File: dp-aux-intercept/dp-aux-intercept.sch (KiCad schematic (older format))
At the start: 29 parts

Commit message: Assigning footprints to AUX select headers.
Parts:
- JCAUXN1, JCAUXP1, JDAUXN1, JDAUXP1: footprint (none) -> Pin_Headers:Pin_Header_Straight_1x03
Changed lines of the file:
@@
 F 0 "JCAUXP1" V 3950 4340 50  0000 C CNN
 F 1 "CONN_01X03" V 3950 4340 50  0001 C CNN
-F 2 "" H 3850 4340 60  0001 C CNN
+F 2 "Pin_Headers:Pin_Header_Straight_1x03" H 3850 4340 60  0001 C CNN
 F 3 "" H 3850 4340 60  0000 C CNN
 	1    3850 4340
@@
 F 0 "JCAUXN1" V 3950 5080 50  0000 C CNN
 F 1 "CONN_01X03" V 3950 5080 50  0001 C CNN
-F 2 "" H 3850 5080 60  0001 C CNN
+F 2 "Pin_Headers:Pin_Header_Straight_1x03" H 3850 5080 60  0001 C CNN
 F 3 "" H 3850 5080 60  0000 C CNN
 	1    3850 5080
@@
 F 0 "JDAUXP1" V 5880 4340 50  0000 C CNN
 F 1 "CONN_01X03" V 5890 4340 50  0001 C CNN
-F 2 "" H 5790 4340 60  0001 C CNN
+F 2 "Pin_Headers:Pin_Header_Straight_1x03" H 5790 4340 60  0001 C CNN
 F 3 "" H 5790 4340 60  0000 C CNN
 	1    5790 4340
@@
 F 0 "JDAUXN1" V 5880 5080 50  0000 C CNN
 F 1 "CONN_01X03" V 5890 5080 50  0001 C CNN
-F 2 "" H 5790 5080 60  0001 C CNN
+F 2 "Pin_Headers:Pin_Header_Straight_1x03" H 5790 5080 60  0001 C CNN
 F 3 "" H 5790 5080 60  0000 C CNN
 	1    5790 5080

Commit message: Temp commit.
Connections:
- net CAUX_N is gone; now on net CAUX1_N: CCAN1.2, DPC1.17 (AUXCH_N), RCAN1.2
- net CAUX_P is gone; now on net CAUX1_P: CCAP1.2, DPC1.15 (AUXCH_P), RCAP1.1
- net DAUX_N is gone; now on net DAUX1_N: CDAN1.1, DPD1.17 (AUXCH_N), RDAN1.2
- net DAUX_P is gone; now on net DAUX1_P: CDAP1.1, DPD1.15 (AUXCH_P), RDAP1.1
- net CAUX2_P: now reaches CCAP1.1, JCAUXP1.2 (P2), RCAP2.1
- net CAUX2_N: now reaches CCAN1.1, JCAUXN1.2 (P2), RCAN2.2
- net DAUX2_P: now reaches CDAP1.2, JDAUXP1.2 (P2), RDAP2.1
- net DAUX2_N: now reaches CDAN1.2, JDAUXN1.2 (P2), RDAN2.2
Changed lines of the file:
@@
 Text Label 2050 2640 0    60   ~ 0
 CAUX_P
-Text Label 2500 5080 0    60   ~ 0
-CAUX_N
+Text Label 2500 5080 0    39   ~ 0
+CAUX1_N
 Text Label 7270 2640 0    60   ~ 0
 DAUX_P
@@
 	0    -1   -1   0
 $EndComp
-Text Notes 2780 4200 0    60   ~ 0
+Text Notes 2710 4130 0    60   ~ 0
 DisplayPort Sink\n    Biasing
 Text Notes 760  930  0    60   ~ 0
@@
 Wire Wire Line
 	2480 2640 2480 4340
-Text Label 2500 4340 0    60   ~ 0
-CAUX_P
+Text Label 2500 4340 0    39   ~ 0
+CAUX1_P
 $Comp
 L VDD #PWR08
@@
 	5700 4740 5700 4540
 Connection ~ 5700 4540
-Text Label 6860 4340 0    60   ~ 0
-DAUX_P
-Text Label 6860 5080 0    60   ~ 0
-DAUX_N
-Text Notes 6110 4210 0    60   ~ 0
+Text Label 6860 4340 0    39   ~ 0
+DAUX1_P
+Text Label 6860 5080 0    39   ~ 0
+DAUX1_N
+Text Notes 6220 4170 0    60   ~ 0
 DisplayPort Source\n      Biasing
 Connection ~ 7630 3040
@@
 Text Label 4290 3840 0    60   ~ 0
 CHPD
+Text Label 3480 4340 1    39   ~ 0
+CAUX2_P
+Text Label 3490 5080 3    39   ~ 0
+CAUX2_N
+Text Label 6180 5080 3    39   ~ 0
+DAUX2_N
+Text Label 6170 4340 1    39   ~ 0
+DAUX2_P
 $EndSCHEMATC

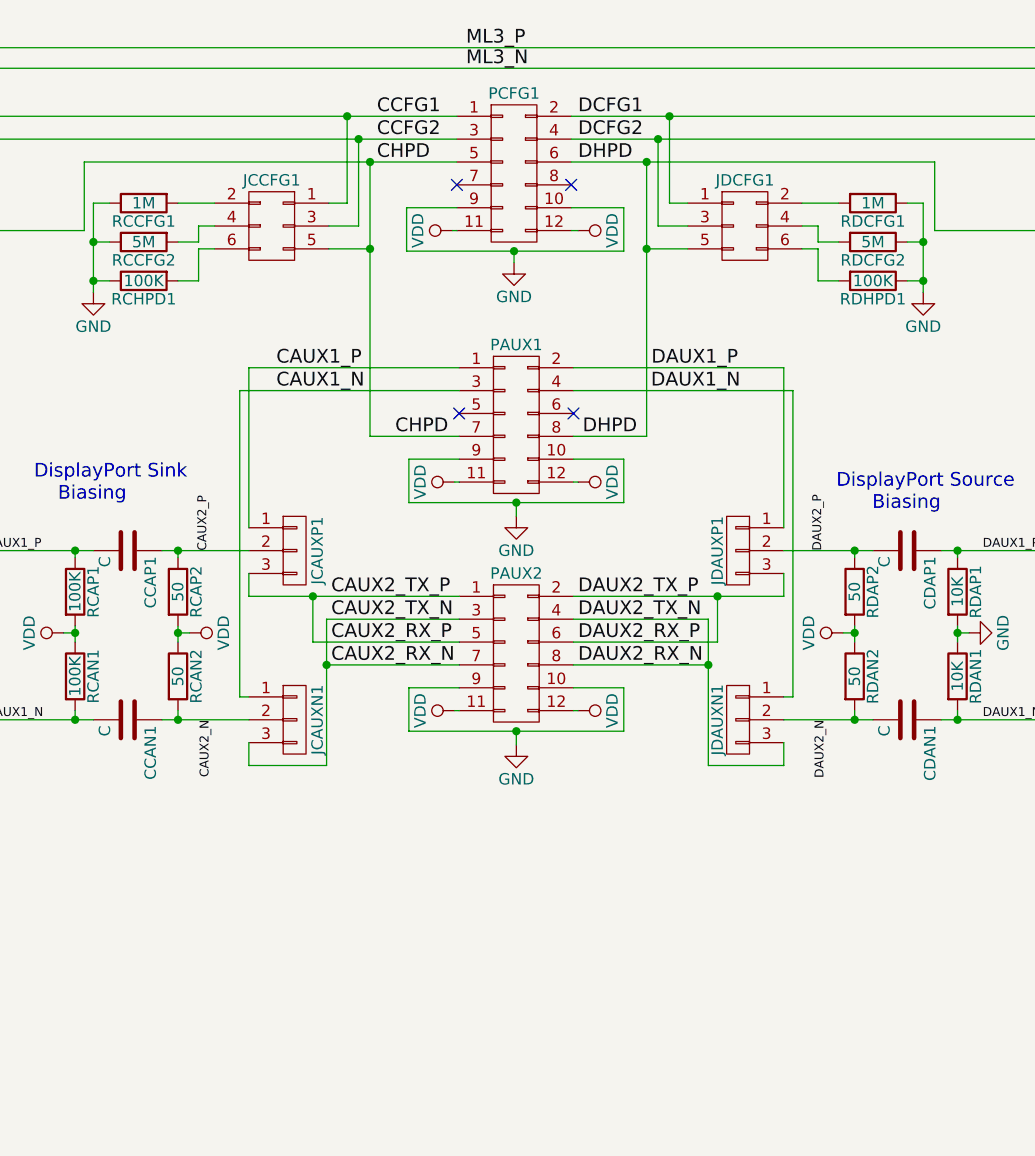
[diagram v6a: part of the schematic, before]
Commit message: Alternative method of two PMOD styles.
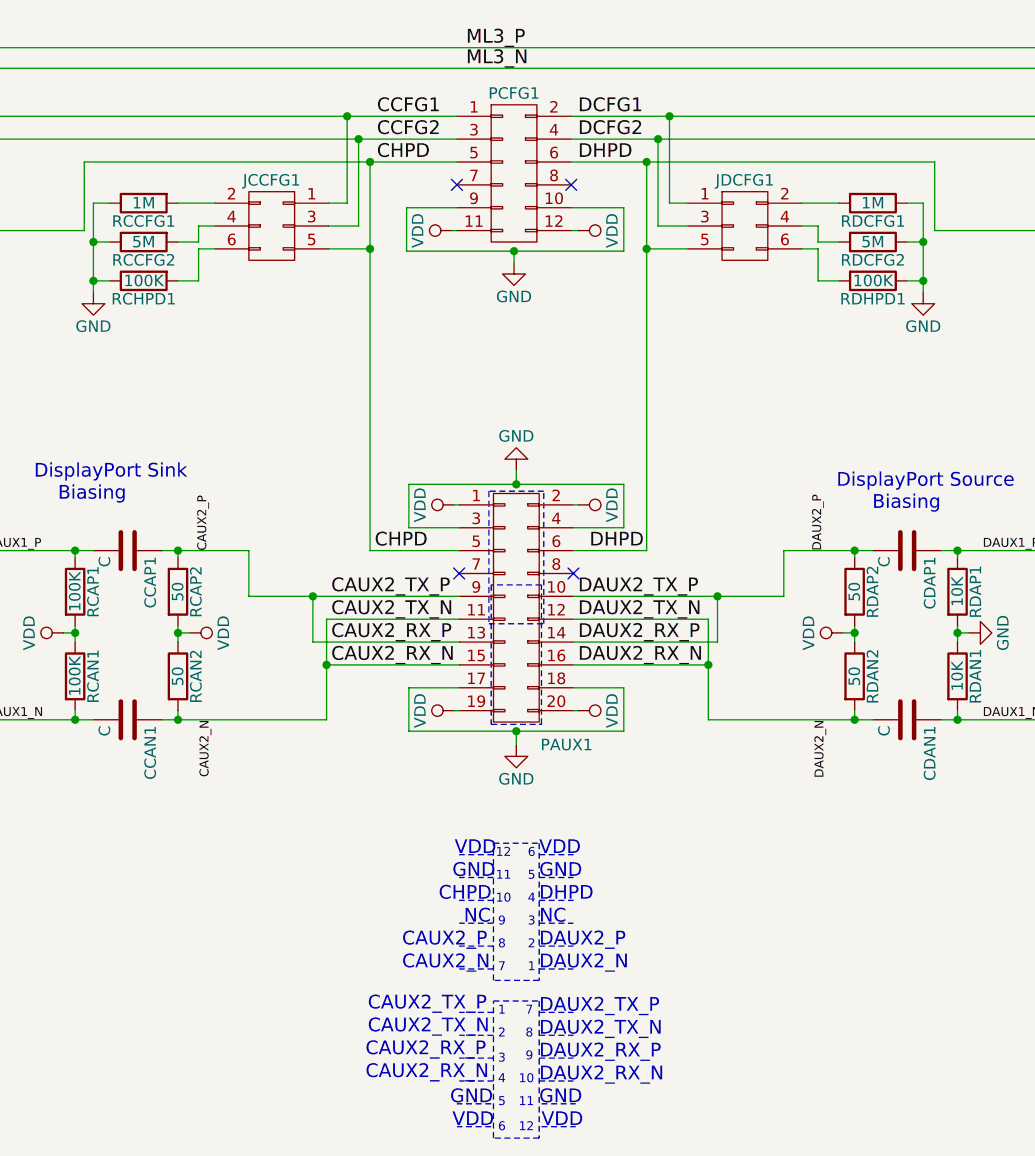
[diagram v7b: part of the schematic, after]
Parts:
- removed JCAUXN1, JCAUXP1, JDAUXN1, JDAUXP1: CONN_01X03, Pin_Headers:Pin_Header_Straight_1x03, symbol CONN_01X03
- removed PAUX1, PAUX2: CONN_02X06, Pin_Headers:Pin_Header_Angled_2x06, symbol CONN_02X06
- added PAUX1: CONN_02X10, Socket_Strips:Socket_Strip_Angled_2x10, symbol CONN_02X10
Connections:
- net CAUX2_N: now also PAUX1.11 (P11), PAUX1.15 (P15)
- net CAUX2_P: now also PAUX1.13 (P13), PAUX1.9 (P9)
- net CHPD: now also PAUX1.5 (P5)
- net DAUX2_N: now also PAUX1.12 (P12), PAUX1.16 (P16)
- net DAUX2_P: now also PAUX1.10 (P10), PAUX1.14 (P14)
- net DHPD: now also PAUX1.6 (P6)
- net GND: now also PAUX1.17 (P17), PAUX1.18 (P18), PAUX1.3 (P3), PAUX1.4 (P4)
- net VDD: now also PAUX1.1 (P1), PAUX1.19 (P19), PAUX1.2 (P2), PAUX1.20 (P20)
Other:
- note added: "1"
- note added: "10"
- note added: "11"
- note added: "12"
- note added: "2"
- note added: "3"
- note added: "4"
- note added: "5"
- note added: "6"
- note added: "7"
- note added: "8"
- note added: "9"
- note added: "CAUX2_N"
- note added: "CAUX2_P"
- note added: "CAUX2_RX_N"
- note added: "CAUX2_RX_P"
- note added: "CAUX2_TX_N"
- note added: "CAUX2_TX_P"
- note added: "CHPD"
- note added: "DAUX2_N"
- note added: "DAUX2_P"
- note added: "DAUX2_RX_N"
- note added: "DAUX2_RX_P"
- note added: "DAUX2_TX_N"
- note added: "DAUX2_TX_P"
- note added: "DHPD"
- note added: "GND"
- note added: "NC"
- note added: "VDD"

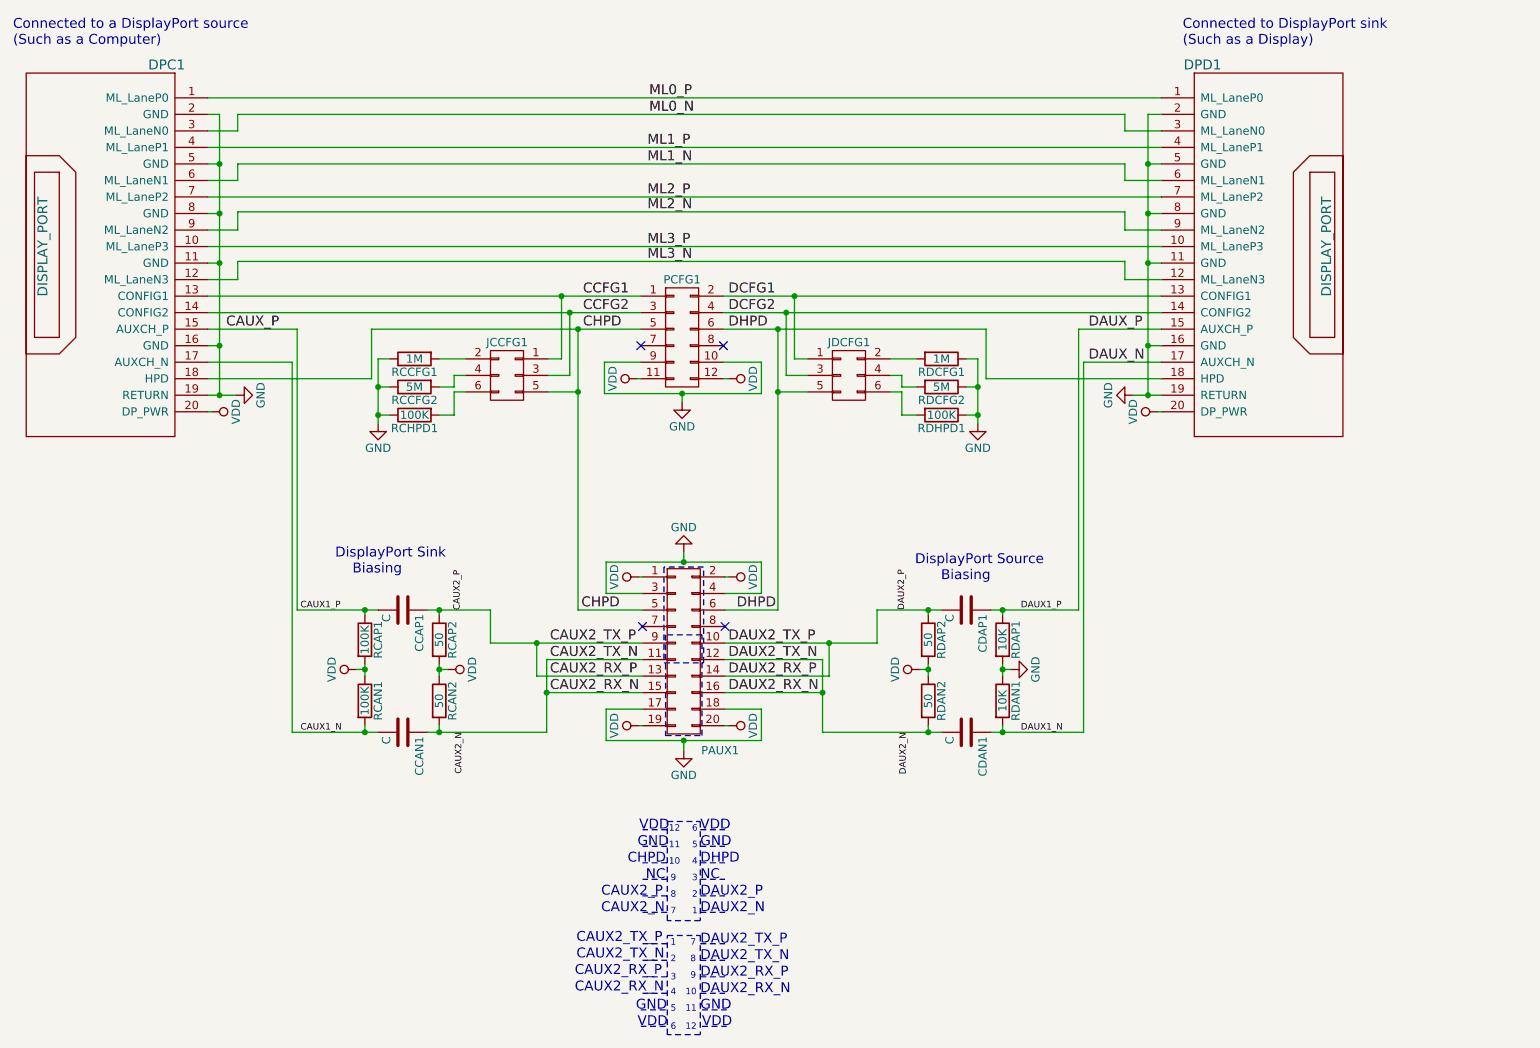
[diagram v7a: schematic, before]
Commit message: Reordering headers to make routing easier.
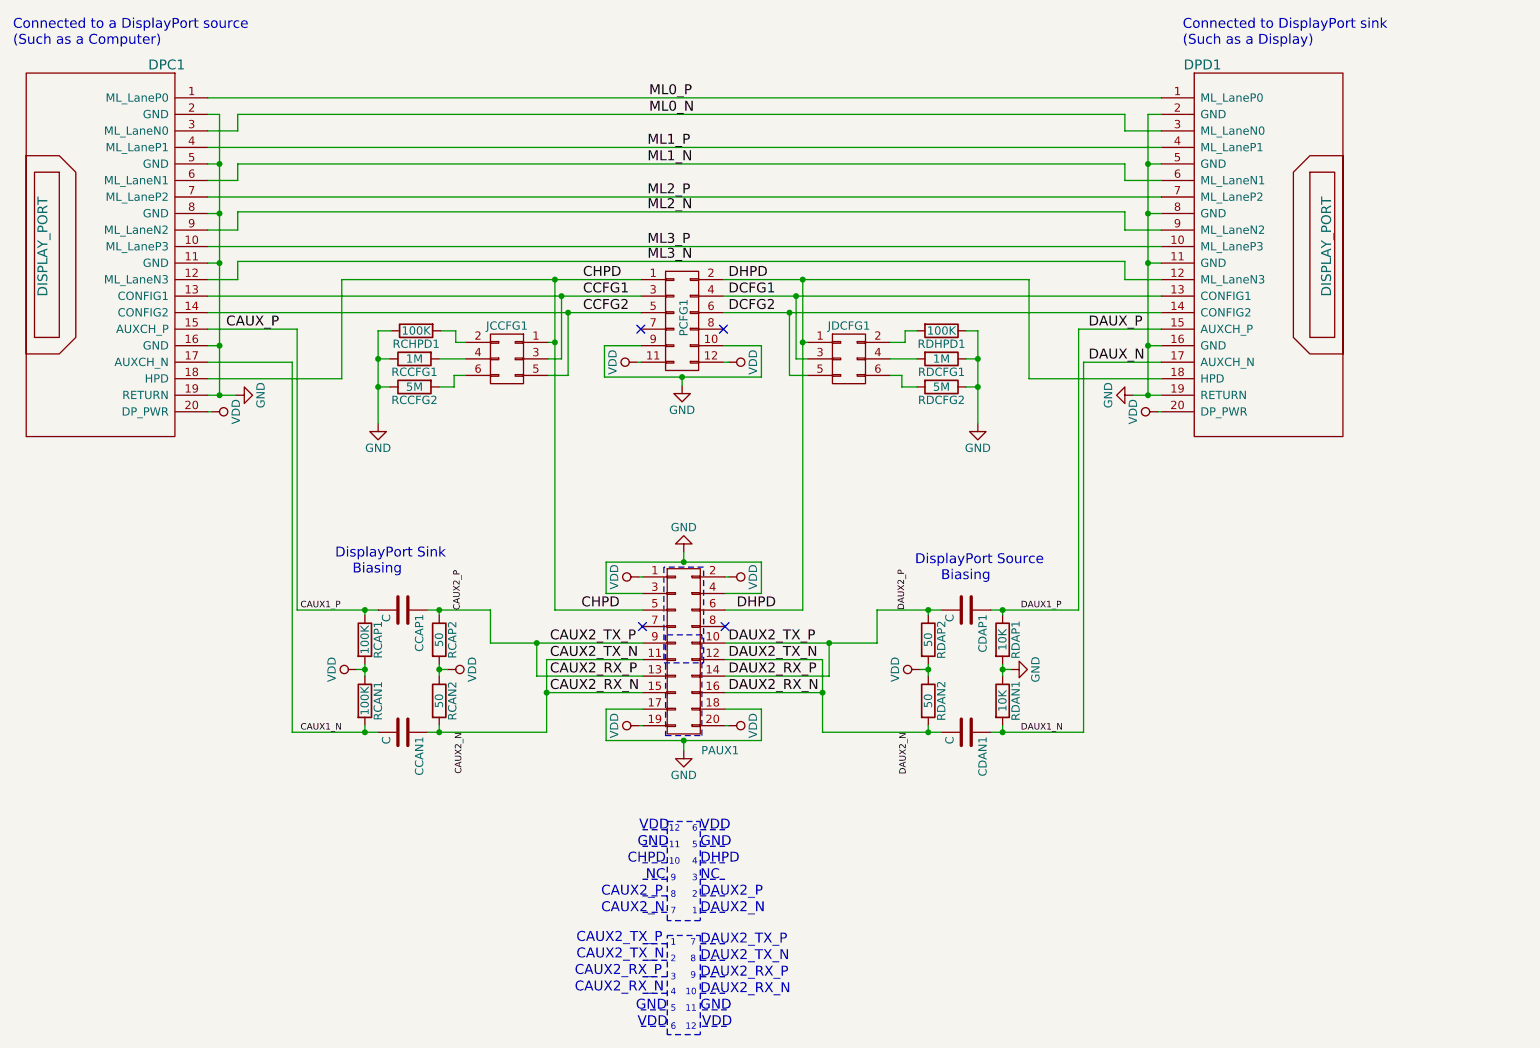
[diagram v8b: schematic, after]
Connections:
- net CCFG1: now also JCCFG1.3 (P3), PCFG1.3 (P3); no longer JCCFG1.1 (P1), PCFG1.1 (P1)
- net CCFG2: now also JCCFG1.5 (P5), PCFG1.5 (P5); no longer JCCFG1.3 (P3), PCFG1.3 (P3)
- net CHPD: now also JCCFG1.1 (P1), PCFG1.1 (P1); no longer JCCFG1.5 (P5), PCFG1.5 (P5)
- net DCFG1: now also JDCFG1.3 (P3), PCFG1.4 (P4); no longer JDCFG1.1 (P1), PCFG1.2 (P2)
- net DCFG2: now also JDCFG1.5 (P5), PCFG1.6 (P6); no longer JDCFG1.3 (P3), PCFG1.4 (P4)
- net DHPD: now also JDCFG1.1 (P1), PCFG1.2 (P2); no longer JDCFG1.5 (P5), PCFG1.6 (P6)
- net at RDCFG1.2: now also JDCFG1.4 (P4); no longer JDCFG1.2 (P2)
- net at RDCFG2.2: now also JDCFG1.6 (P6); no longer JDCFG1.4 (P4)
- net at RDHPD1.2: now also JDCFG1.2 (P2); no longer JDCFG1.6 (P6)
- net at RCCFG1.2: now also JCCFG1.4 (P4); no longer JCCFG1.2 (P2)
- net at RCCFG2.2: now also JCCFG1.6 (P6); no longer JCCFG1.4 (P4)
- net at RCHPD1.2: now also JCCFG1.2 (P2); no longer JCCFG1.6 (P6)
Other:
- moved on the sheet: JCCFG1, JDCFG1, PCFG1, RCHPD1, RDHPD1
